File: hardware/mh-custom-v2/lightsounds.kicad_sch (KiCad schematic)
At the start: 21 parts, among them J1 Conn_01x03_Male, J2 Conn_01x03_Female, SW1 SW_DIP_x04, T1 AO3400A, T2 AO3400A, T5 AO3400A

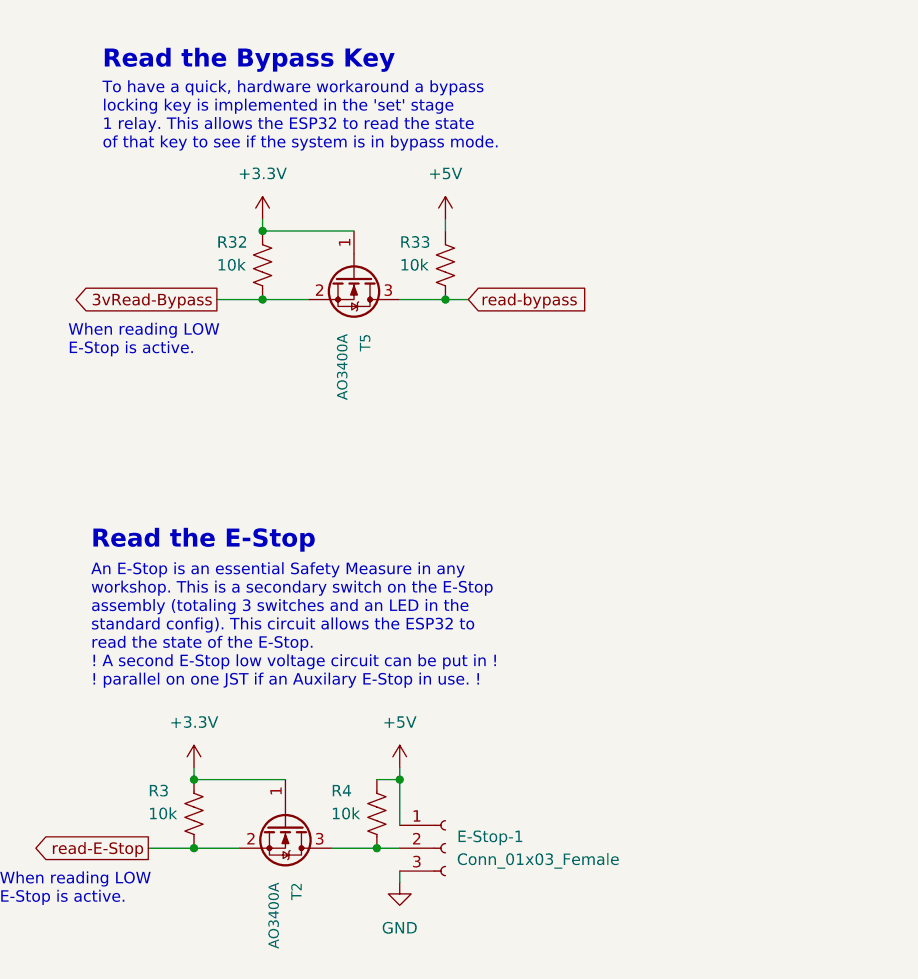
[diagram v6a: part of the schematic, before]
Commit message: added linear regulator for 3.3V peripherals and ADE7953 reset jumper
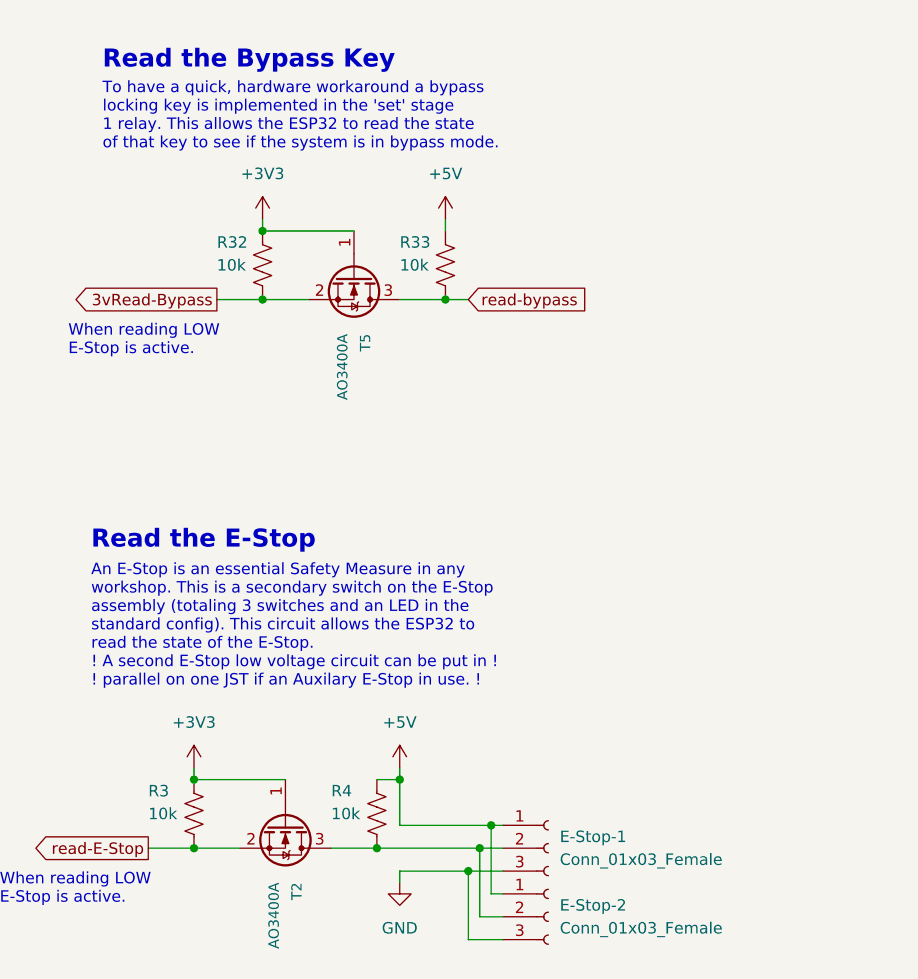
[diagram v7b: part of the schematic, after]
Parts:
- added E-Stop-2: Conn_01x03_Female, Connector_JST:JST_PH_B3B-PH-K_1x03_P2.00mm_Vertical, symbol Connector:Conn_01x03_Female
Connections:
- net +5V: now also E-Stop-2.1 (Pin_1)
- net GND: now also E-Stop-2.3 (Pin_3)
- net at E-Stop-1.2 (Pin_2), R4.1, T2.3 (D): now also E-Stop-2.2 (Pin_2)
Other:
- moved on the sheet: E-Stop-1
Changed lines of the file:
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@@
   (junction (at 82.55 111.76) (diameter 0) (color 0 0 0 0)
   )
+  (junction (at 86.36 172.72) (diameter 0) (color 0 0 0 0)
+  )
   (junction (at 50.8 63.5) (diameter 0) (color 0 0 0 0)
   )
@@
   (junction (at 160.02 77.47) (diameter 0) (color 0 0 0 0)
   )
+  (junction (at 54.61 165.1) (diameter 0) (color 0 0 0 0)
+  )
+  (junction (at 74.93 172.72) (diameter 0) (color 0 0 0 0)
+  )
+  (junction (at 87.63 170.18) (diameter 0) (color 0 0 0 0)
+  )
   (junction (at 77.47 165.1) (diameter 0) (color 0 0 0 0)
   )
-  (junction (at 54.61 165.1) (diameter 0) (color 0 0 0 0)
-  )
-  (junction (at 74.93 172.72) (diameter 0) (color 0 0 0 0)
-  )
   (junction (at 250.19 152.4) (diameter 0) (color 0 0 0 0)
   )
+  (junction (at 85.09 175.26) (diameter 0) (color 0 0 0 0)
+  )
   (wire (pts (xy 68.58 55.88) (xy 69.85 55.88))
     (stroke (width 0) (type default) (color 0 0 0 0))
@@
     (stroke (width 0) (type default) (color 0 0 0 0))
   )
+  (wire (pts (xy 85.09 175.26) (xy 77.47 175.26))
+    (stroke (width 0) (type default) (color 0 0 0 0))
+  )
   (wire (pts (xy 151.13 68.58) (xy 152.4 68.58))
     (stroke (width 0) (type default) (color 0 0 0 0))
   )
-  (wire (pts (xy 77.47 165.1) (xy 77.47 170.18))
-    (stroke (width 0) (type default) (color 0 0 0 0))
-  )
   (wire (pts (xy 54.61 172.72) (xy 59.69 172.72))
     (stroke (width 0) (type default) (color 0 0 0 0))
@@
     (stroke (width 0) (type default) (color 0 0 0 0))
   )
+  (wire (pts (xy 88.9 182.88) (xy 85.09 182.88))
+    (stroke (width 0) (type default) (color 0 0 0 0))
+  )
   (wire (pts (xy 160.02 73.66) (xy 160.02 77.47))
     (stroke (width 0) (type default) (color 0 0 0 0))
@@
     (stroke (width 0) (type default) (color 0 0 0 0))
   )
+  (wire (pts (xy 87.63 177.8) (xy 87.63 170.18))
+    (stroke (width 0) (type default) (color 0 0 0 0))
+  )
   (wire (pts (xy 77.47 163.83) (xy 77.47 165.1))
     (stroke (width 0) (type default) (color 0 0 0 0))
   )
-  (wire (pts (xy 74.93 172.72) (xy 77.47 172.72))
+  (wire (pts (xy 74.93 172.72) (xy 86.36 172.72))
     (stroke (width 0) (type default) (color 0 0 0 0))
   )
@@
     (stroke (width 0) (type default) (color 0 0 0 0))
   )
+  (wire (pts (xy 86.36 180.34) (xy 86.36 172.72))
+    (stroke (width 0) (type default) (color 0 0 0 0))
+  )
   (wire (pts (xy 62.23 104.14) (xy 72.39 104.14))
     (stroke (width 0) (type default) (color 0 0 0 0))
@@
     (stroke (width 0) (type default) (color 0 0 0 0))
   )
+  (wire (pts (xy 88.9 170.18) (xy 87.63 170.18))
+    (stroke (width 0) (type default) (color 0 0 0 0))
+  )
   (wire (pts (xy 77.47 111.76) (xy 82.55 111.76))
     (stroke (width 0) (type default) (color 0 0 0 0))
@@
     (stroke (width 0) (type default) (color 0 0 0 0))
   )
+  (wire (pts (xy 86.36 172.72) (xy 88.9 172.72))
+    (stroke (width 0) (type default) (color 0 0 0 0))
+  )
   (wire (pts (xy 74.93 165.1) (xy 77.47 165.1))
     (stroke (width 0) (type default) (color 0 0 0 0))
@@
     (stroke (width 0) (type default) (color 0 0 0 0))
   )
+  (wire (pts (xy 85.09 182.88) (xy 85.09 175.26))
+    (stroke (width 0) (type default) (color 0 0 0 0))
+  )
   (wire (pts (xy 53.34 58.42) (xy 50.8 58.42))
     (stroke (width 0) (type default) (color 0 0 0 0))
@@
     (stroke (width 0) (type default) (color 0 0 0 0))
   )
+  (wire (pts (xy 77.47 170.18) (xy 77.47 165.1))
+    (stroke (width 0) (type default) (color 0 0 0 0))
+  )
   (wire (pts (xy 54.61 165.1) (xy 64.77 165.1))
     (stroke (width 0) (type default) (color 0 0 0 0))
@@
     (stroke (width 0) (type default) (color 0 0 0 0))
   )
+  (wire (pts (xy 88.9 177.8) (xy 87.63 177.8))
+    (stroke (width 0) (type default) (color 0 0 0 0))
+  )
+  (wire (pts (xy 87.63 170.18) (xy 77.47 170.18))
+    (stroke (width 0) (type default) (color 0 0 0 0))
+  )
   (wire (pts (xy 69.85 63.5) (xy 68.58 63.5))
     (stroke (width 0) (type default) (color 0 0 0 0))
@@
     (stroke (width 0) (type default) (color 0 0 0 0))
   )
+  (wire (pts (xy 88.9 175.26) (xy 85.09 175.26))
+    (stroke (width 0) (type default) (color 0 0 0 0))
+  )
   (wire (pts (xy 62.23 102.87) (xy 62.23 104.14))
     (stroke (width 0) (type default) (color 0 0 0 0))
@@
   )
   (wire (pts (xy 62.23 111.76) (xy 67.31 111.76))
+    (stroke (width 0) (type default) (color 0 0 0 0))
+  )
+  (wire (pts (xy 88.9 180.34) (xy 86.36 180.34))
     (stroke (width 0) (type default) (color 0 0 0 0))
   )
@@
     (pin "1")
   )
-  (symbol (lib_id "power:+3.3V") (at 62.23 102.87 0) (unit 1)
-    (in_bom yes) (on_board yes) (fields_autoplaced)
-    (property "Reference" "#PWR01" (id 0) (at 62.23 106.68 0)
-      (effects (font (size 1.27 1.27)) hide)
-    )
-    (property "Value" "+3.3V" (id 1) (at 62.23 97.79 0))
+  (symbol (lib_id "power:+3V3") (at 62.23 102.87 0) (unit 1)
+    (in_bom yes) (on_board yes) (fields_autoplaced)
+    (property "Reference" "#PWR04" (id 0) (at 62.23 106.68 0)
+      (effects (font (size 1.27 1.27)) hide)
+    )
+    (property "Value" "+3V3" (id 1) (at 62.23 97.79 0))
     (property "Footprint" "" (id 2) (at 62.23 102.87 0)
       (effects (font (size 1.27 1.27)) hide)
@@
     (pin "3")
   )
+  (symbol (lib_id "power:+3V3") (at 54.61 163.83 0) (unit 1)
+    (in_bom yes) (on_board yes) (fields_autoplaced)
+    (property "Reference" "#PWR03" (id 0) (at 54.61 167.64 0)
+      (effects (font (size 1.27 1.27)) hide)
+    )
+    (property "Value" "+3V3" (id 1) (at 54.61 158.75 0))
+    (property "Footprint" "" (id 2) (at 54.61 163.83 0)
+      (effects (font (size 1.27 1.27)) hide)
+    )
+    (property "Datasheet" "" (id 3) (at 54.61 163.83 0)
+      (effects (font (size 1.27 1.27)) hide)
+    )
+    (pin "1")
+  )
   (symbol (lib_id "power:GND") (at 207.01 152.4 0) (unit 1)
     (in_bom yes) (on_board yes) (fields_autoplaced)
@@
     (pin "3")
   )
+  (symbol (lib_id "Connector:Conn_01x03_Female") (at 93.98 180.34 0) (unit 1)
+    (in_bom yes) (on_board yes) (fields_autoplaced)
+    (property "Reference" "E-Stop-2" (id 0) (at 95.25 179.0699 0)
+      (effects (font (size 1.27 1.27)) (justify left))
+    )
+    (property "Value" "Conn_01x03_Female" (id 1) (at 95.25 181.6099 0)
+      (effects (font (size 1.27 1.27)) (justify left))
+    )
+    (property "Footprint" "Connector_JST:JST_PH_B3B-PH-K_1x03_P2.00mm_Vertical" (id 2) (at 93.98 180.34 0)
+      (effects (font (size 1.27 1.27)) hide)
+    )
+    (property "Datasheet" "~" (id 3) (at 93.98 180.34 0)
+      (effects (font (size 1.27 1.27)) hide)
+    )
+    (property "JLCPCB Part #" "C131339" (id 4) (at 93.98 180.34 0)
+      (effects (font (size 1.27 1.27)) hide)
+    )
+    (pin "1")
+    (pin "2")
+    (pin "3")
+  )
   (symbol (lib_id "Connector:Conn_01x02_Female") (at 212.09 144.78 0) (unit 1)
     (in_bom yes) (on_board yes) (fields_autoplaced)
@@
     (pin "1")
   )
-  (symbol (lib_id "power:+3.3V") (at 54.61 163.83 0) (unit 1)
-    (in_bom yes) (on_board yes) (fields_autoplaced)
-    (property "Reference" "#PWR0109" (id 0) (at 54.61 167.64 0)
-      (effects (font (size 1.27 1.27)) hide)
-    )
-    (property "Value" "+3.3V" (id 1) (at 54.61 158.75 0))
-    (property "Footprint" "" (id 2) (at 54.61 163.83 0)
-      (effects (font (size 1.27 1.27)) hide)
-    )
-    (property "Datasheet" "" (id 3) (at 54.61 163.83 0)
-      (effects (font (size 1.27 1.27)) hide)
-    )
-    (pin "1")
-  )
   (symbol (lib_id "Connector:Conn_01x02_Female") (at 255.27 144.78 0) (unit 1)
     (in_bom yes) (on_board yes) (fields_autoplaced)
@@
     (pin "3")
   )
-  (symbol (lib_id "Connector:Conn_01x03_Female") (at 82.55 172.72 0) (unit 1)
-    (in_bom yes) (on_board yes) (fields_autoplaced)
-    (property "Reference" "E-Stop-1" (id 0) (at 83.82 171.4499 0)
-      (effects (font (size 1.27 1.27)) (justify left))
-    )
-    (property "Value" "Conn_01x03_Female" (id 1) (at 83.82 173.9899 0)
-      (effects (font (size 1.27 1.27)) (justify left))
-    )
-    (property "Footprint" "Connector_JST:JST_PH_B3B-PH-K_1x03_P2.00mm_Vertical" (id 2) (at 82.55 172.72 0)
-      (effects (font (size 1.27 1.27)) hide)
-    )
-    (property "Datasheet" "~" (id 3) (at 82.55 172.72 0)
-      (effects (font (size 1.27 1.27)) hide)
-    )
-    (property "JLCPCB Part #" "C131339" (id 4) (at 82.55 172.72 0)
-      (effects (font (size 1.27 1.27)) hide)
-    )
+  (symbol (lib_id "Connector:Conn_01x03_Female") (at 93.98 172.72 0) (unit 1)
+    (in_bom yes) (on_board yes) (fields_autoplaced)
+    (property "Reference" "E-Stop-1" (id 0) (at 95.25 171.4499 0)
+      (effects (font (size 1.27 1.27)) (justify left))
+    )
+    (property "Value" "Conn_01x03_Female" (id 1) (at 95.25 173.9899 0)
+      (effects (font (size 1.27 1.27)) (justify left))
+    )
+    (property "Footprint" "Connector_JST:JST_PH_B3B-PH-K_1x03_P2.00mm_Vertical" (id 2) (at 93.98 172.72 0)
+      (effects (font (size 1.27 1.27)) hide)
+    )
+    (property "Datasheet" "~" (id 3) (at 93.98 172.72 0)
+      (effects (font (size 1.27 1.27)) hide)
+    )
+    (property "JLCPCB Part #" "C131339" (id 4) (at 93.98 172.72 0)
+      (effects (font (size 1.27 1.27)) hide)
+    )

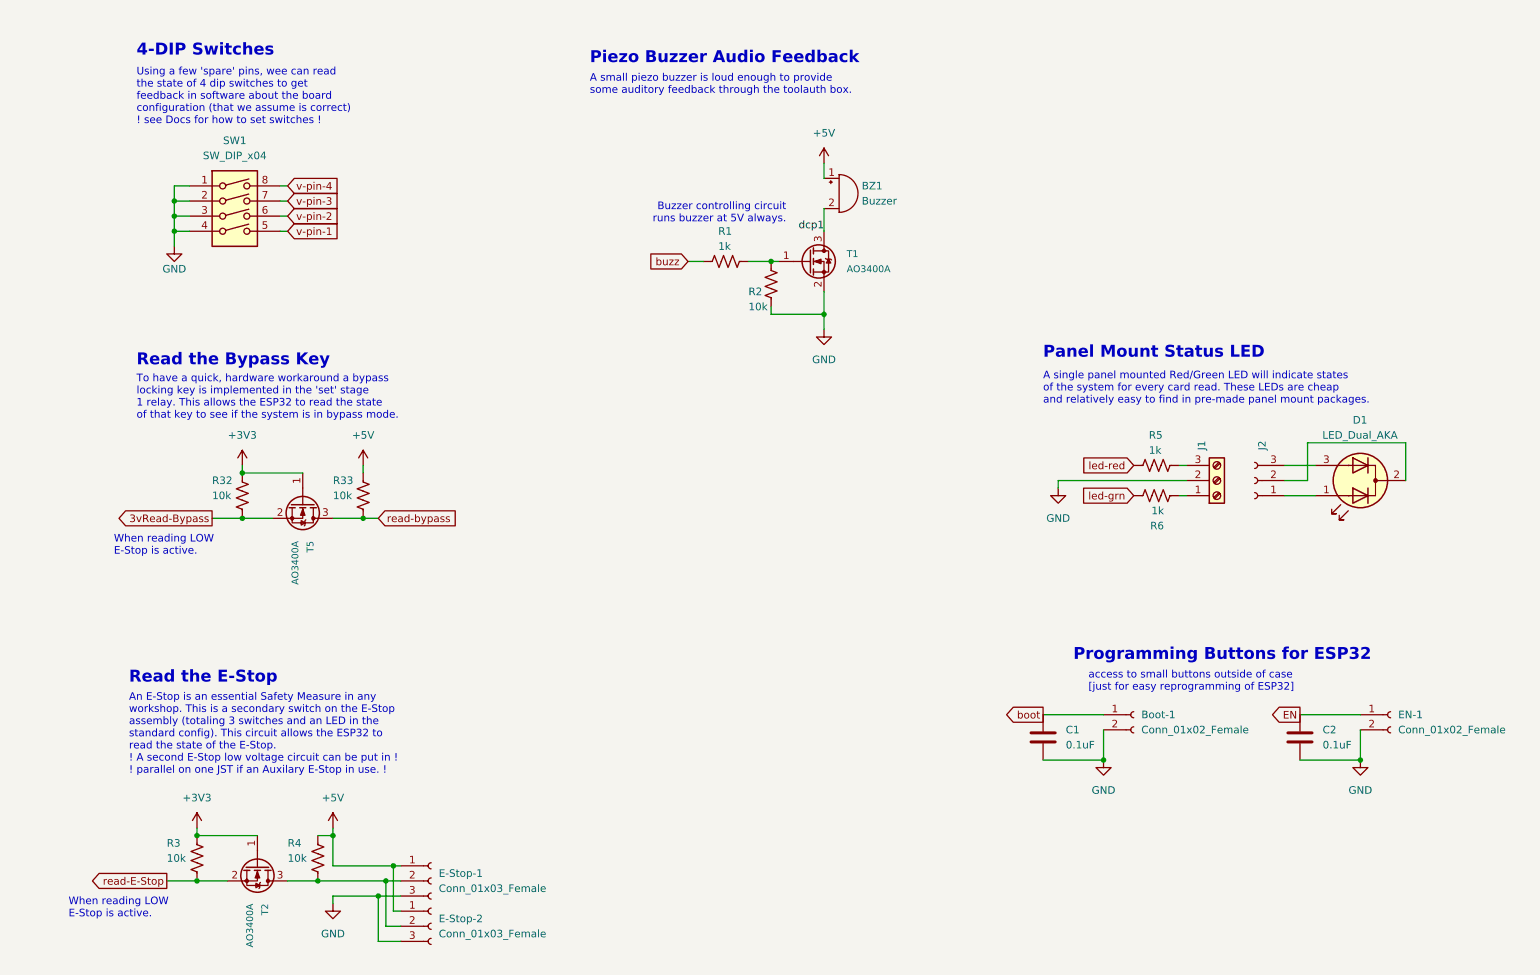
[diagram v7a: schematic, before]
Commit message: added jumpers that allow for two seperate E-Stop readings
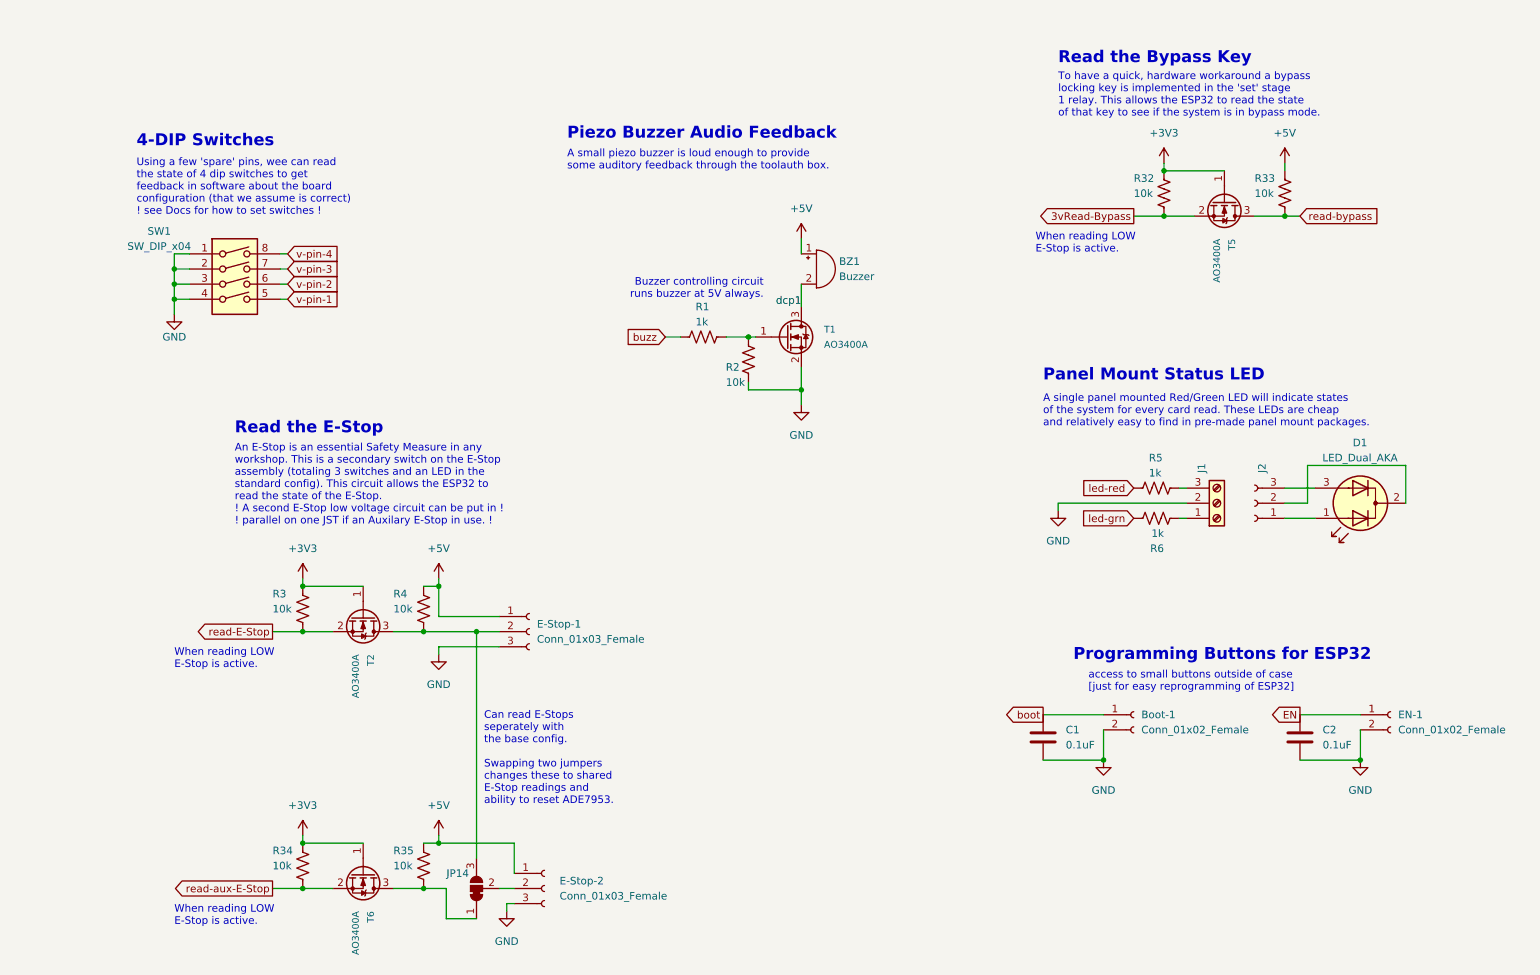
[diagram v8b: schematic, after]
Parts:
- added JP14: SolderJumper_3_Bridged12, Jumper:SolderJumper-3_P1.3mm_Bridged12_RoundedPad1.0x1.5mm, symbol Jumper:SolderJumper_3_Bridged12
- added R34, R35: 10k, Resistor_SMD:R_0603_1608Metric, symbol Device:R_US
- added T6: AO3400A, Package_TO_SOT_SMD:SOT-23, symbol Transistor_FET:AO3400A
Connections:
- net +3V3: now also R34.2, T6.1 (G)
- net +5V: now also R35.2
- net at E-Stop-1.2 (Pin_2), R4.1, T2.3 (D): now also JP14.3 (B); no longer E-Stop-2.2 (Pin_2)
- new net: JP14.1 (A), R35.1, T6.3 (D)
- new net: E-Stop-2.2 (Pin_2), JP14.2 (C)
- new net read-aux-E-Stop: R34.1, T6.2 (S)
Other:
- note added: "Can read E-Stops seperately with the base config. Swapping two jumpers changes these to shared E-Stop readings and ability to reset ADE7953."
- moved on the sheet: BZ1, D1, E-Stop-1, E-Stop-2, J1, J2, R1, R2, R3, R32, R33, R4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
